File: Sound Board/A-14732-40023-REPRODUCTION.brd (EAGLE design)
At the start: 160 x 100 mm, 220 parts, among them P6 POWER, P7 SPEAKER, Q1 MPS3646, U1 OKI6295, U10 26LS32A, U11 26LS31, U12 27C040-150, U13 27C040-150, U14 YAMAHA 2151, U15 TIL7524, U16 74LS374, U17 74LS174, U18 16L8, U19 74LS11, U2 2064, U20 74LS139, U21 74LS14, U22 74LS74, U23 74LS74, U24 26LS31, U25 26LS32A, U26 74LS04, U28 YAMAHA 3012, U29 LM324D, U3 27C040, U30 MC3340, U31 MB3731, U32 TL084D, U33 TL084D, U4 6809E, U5 74LS374DW, U6 26LS32A, U7 26LS31, U8 74LS138, U9 74LS74, Y1 3.5749MHz, Y2 8MHz

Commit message: initial layout after autogeneration
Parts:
- VR1: device MK-ICs:7809-D2PAK -> MK-ICs:7809-TO220V
- moved P1 281.2 mm to (156.2, 76.2), turned to 270 degrees
- moved MTG1 271.6 mm to (158.8, 2.54)
- moved U31 268.3 mm to (157.5, 30.5), turned to 270 degrees
- moved MTG3 261.1 mm to (157.5, 96.5)
- moved L1 259.8 mm to (128.3, 17.8)
- moved L2 257.4 mm to (116.8, 17.8)
- moved RV1 239.1 mm to (105.4, 6.35), turned to 90 degrees
- moved U33 238.5 mm to (139.7, 47.0), turned to 270 degrees
- moved U18 237.8 mm to (119.4, 54.6), turned to 270 degrees
- moved U16 235.0 mm to (138.4, 61.0), turned to 270 degrees
- moved C95 230.5 mm to (137.2, 31.8), turned to 90 degrees
- moved U10 225.7 mm to (156.2, 52.1), turned to 270 degrees
- moved P7 223.8 mm to (149.9, 5.08)
- moved U5 218.7 mm to (137.2, 78.7), turned to 270 degrees
- moved U32 215.9 mm to (129.5, 47.0), turned to 270 degrees
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
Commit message: layout WIP
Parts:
- removed C79: 220uF, A-14732-40023:PANASONIC_E
- added C84: 220uF, A-14732-40023:PANASONIC_E
- RV1: device SparkFun-Electromechanical:ALPS_POT_KIT -> SparkFun-Electromechanical:POT_ALPHA_RV16AF-20
- U1: device MK-ICs:OKI6295 -> A-14732-40023:QFP44
- U12, U13, U3: device MK-ICs:27C040 -> A-14732-40023:PLCC-S32
- U14: device MK-ICs:YM2151 -> A-14732-40023:DIP24
- U18: device MK-ICs:16L8 -> A-14732-40023:DIP20N
- U2: device MK-ICs:MS6264L -> A-14732-40023:SOP28
- U28: device MK-ICs:YM3012 -> A-14732-40023:DIP16N
- Y1: device crystal:SM49 -> crystal:HC49U-V
- moved R92 133.6 mm to (148.8, 43.9), turned to 90 degrees
- moved R18 133.0 mm to (147.3, 63.2)
- moved C43 131.7 mm to (147.3, 66.0), turned to 180 degrees
- moved C48 130.4 mm to (4.57, 9.65)
- moved R17 129.6 mm to (147.8, 68.6)
- moved C42 129.1 mm to (147.8, 71.1), turned to 180 degrees
- moved R16 126.0 mm to (148.1, 73.2)
- moved C41 125.5 mm to (147.3, 74.7), turned to 180 degrees
- moved C47 124.9 mm to (12.7, 95.2)
- moved C12 124.1 mm to (7.87, 85.6)
- moved R15 122.6 mm to (147.6, 79.5), turned to 180 degrees
- moved C40 122.5 mm to (147.6, 77.0), turned to 180 degrees
- moved C7 121.9 mm to (128.8, 98.8), turned to 180 degrees
- moved C50 121.2 mm to (4.83, 15.0)
- moved C83 120.3 mm to (153.4, 43.4)
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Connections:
- net AGND: now also C84.-, RV1.1, RV1.2; no longer C79.-, RV1.P$2, RV1.P$3
- net N$87: now also RV1.3; no longer RV1.P$1
- net N$92: now also C84.+; no longer C79.+
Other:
- board size 160 x 100 mm -> 160 x 102.3 mm

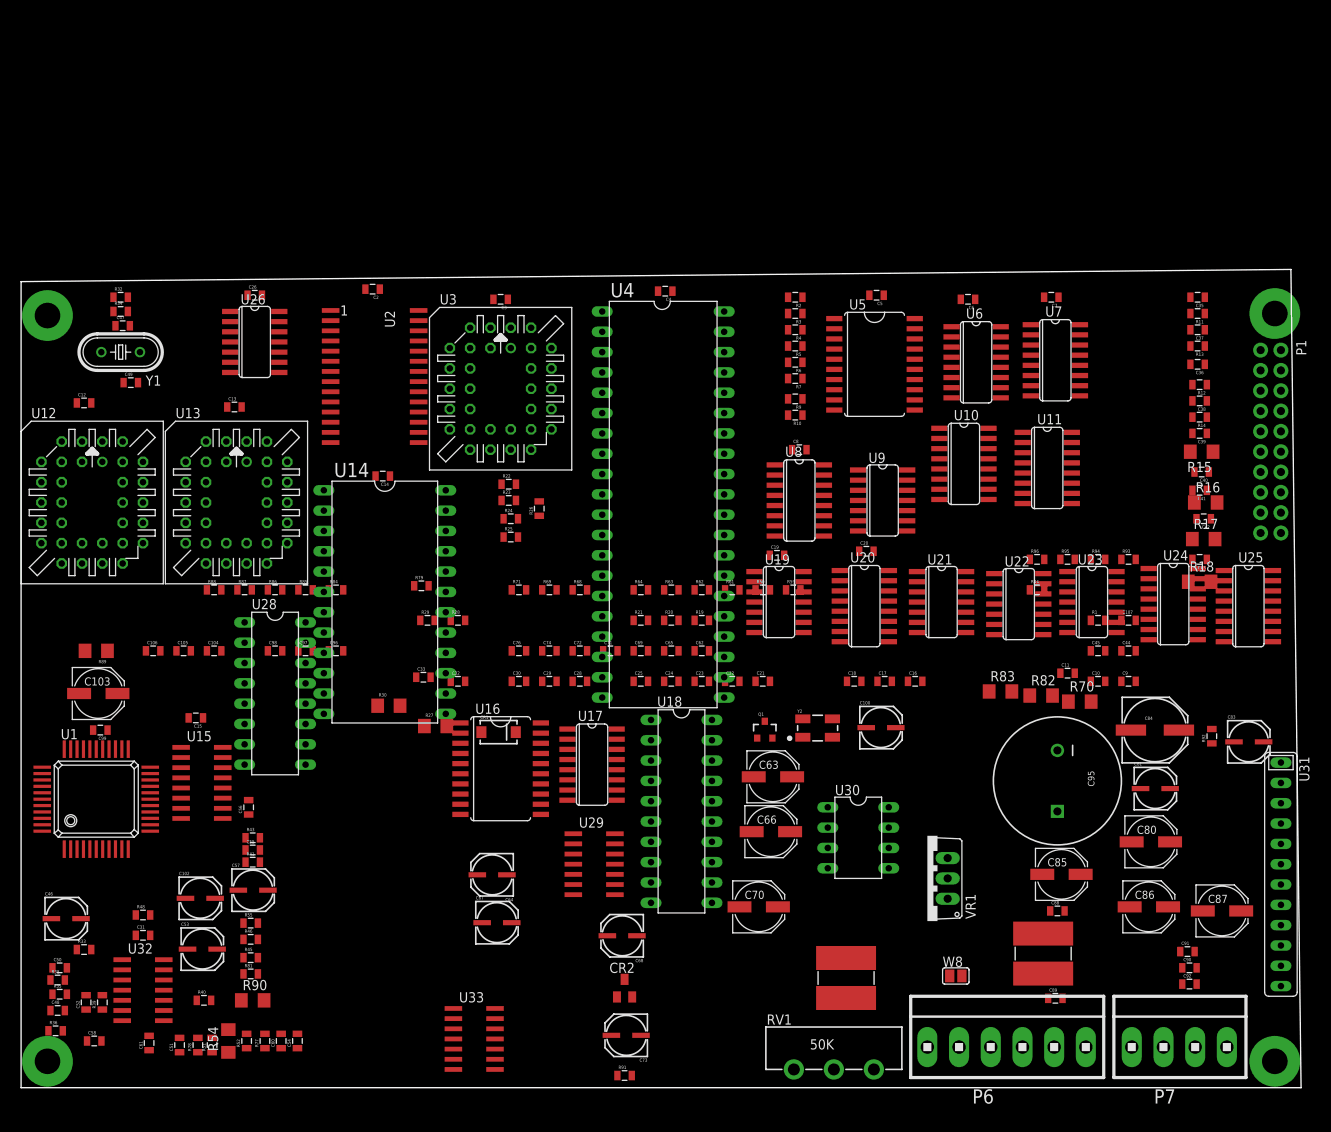
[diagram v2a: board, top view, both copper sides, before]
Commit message: Trying to lay around, resulting in fixing misplaced components and other fixes
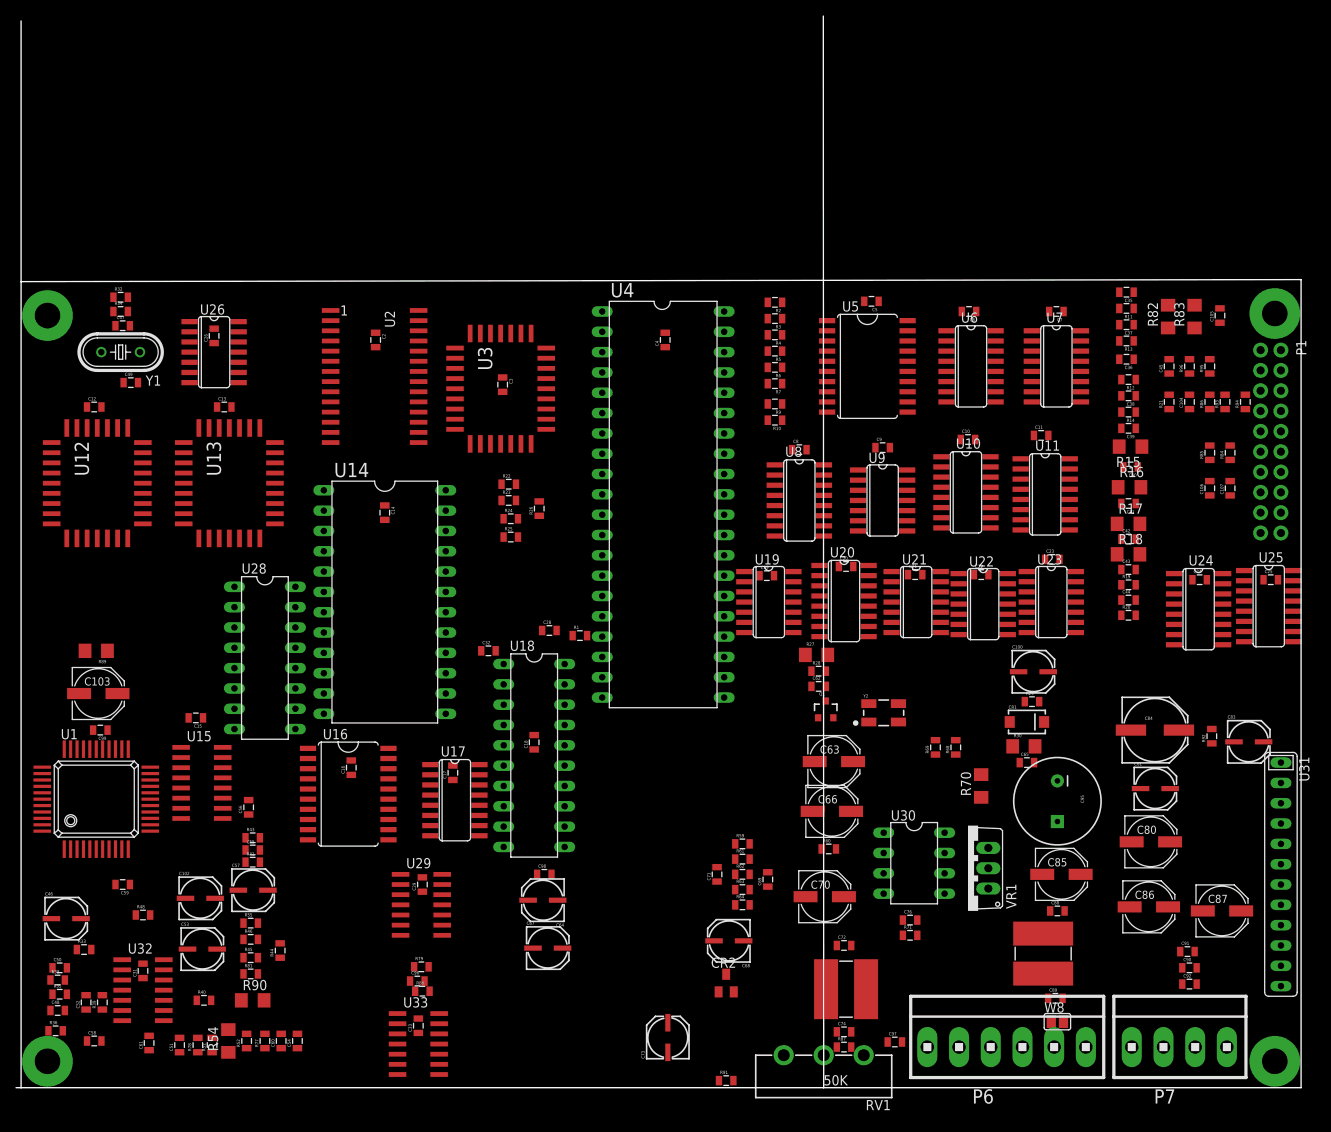
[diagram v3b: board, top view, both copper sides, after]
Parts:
- removed C30: 33pF, SparkFun-Passives:0805
- added C59: 33pF, SparkFun-Passives:0805
- C95: device A-14732-40023:CPOL-RADIAL-1000UF-63V -> A-14732-40023:CPOL-RADIAL-1000UF-25V
- U12, U13, U3: device A-14732-40023:PLCC-S32 -> A-14732-40023:PLCC32R
- moved C105 136.2 mm to (149.9, 96.5), turned to 90 degrees
- moved C106 133.6 mm to (148.6, 74.9), turned to 90 degrees
- moved C104 125.8 mm to (146.1, 85.7), turned to 90 degrees
- moved R86 119.2 mm to (148.6, 85.7), turned to 90 degrees
- moved R85 114.3 mm to (148.6, 79.4), turned to 90 degrees
- moved R84 113.1 mm to (151.1, 79.4), turned to 90 degrees
- moved R44 104.8 mm to (32.4, 17.1), turned to 90 degrees
- moved R87 94.2 mm to (102.9, 5.08)
- moved C97 88.4 mm to (109.2, 5.71)
- moved C25 79.8 mm to (156.2, 63.5)
- moved R30 79.5 mm to (125.3, 42.7)
- moved R29 76.2 mm to (126.4, 48.3)
- moved R21 71.5 mm to (143.5, 85.7), turned to 90 degrees
- moved C16 71.3 mm to (41.3, 40.0), turned to 90 degrees
- moved C24 67.3 mm to (147.3, 63.5)
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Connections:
- net N$79: now also C59.1; no longer C30.1
- net N$80: now also C59.2; no longer C30.2
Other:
- board size 160 x 102.3 mm -> 160.6 x 134 mm

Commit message: board layout wip
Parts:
- R15, R16, R17, R18: device resistor:R1206 -> SparkFun-Passives:0805
- Y1: device crystal:HC49U-V -> crystal:HC49UP
- moved C32 78.0 mm to (135.9, 45.7), turned to 270 degrees
- moved R1 53.5 mm to (34.3, 96.5), turned to 270 degrees
- moved C28 38.1 mm to (27.9, 57.1), turned to 90 degrees
- moved R86 27.9 mm to (158.8, 59.7)
- moved C59 26.4 mm to (27.9, 3.81), turned to 90 degrees
- moved C19 24.8 mm to (90.2, 39.4), flipped to the bottom, turned to 90 degrees
- moved R81 23.5 mm to (50.8, 6.35)
- moved R44 23.3 mm to (54.6, 10.2)
- moved R45 23.3 mm to (50.8, 8.89)
- moved R46 23.2 mm to (50.8, 11.4)
- moved R55 23.1 mm to (50.8, 14.0)
- moved C106 23.0 mm to (151.1, 97.8)
- moved C107 23.0 mm to (153.7, 97.8)
- moved R90 23.0 mm to (50.8, 3.81)
- moved C57 22.6 mm to (50.8, 19.1)
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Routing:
- net GND: track 0.00 -> 516.2 mm
- net SND_DAT3: track 0.00 -> 13.0 mm
- net SND_DAT1: track 0.00 -> 13.0 mm
- net SND_DAT4: track 0.00 -> 7.77 mm
- net B_SND_RD: track 0.00 -> 7.77 mm
- net SND_DAT6: track 0.00 -> 7.77 mm
- net SND_DAT2: track 0.00 -> 7.77 mm
- net SND_DAT0: track 0.00 -> 7.77 mm
- net N$101: track 0.00 -> 7.77 mm
- net SND_RDY: track 0.00 -> 6.72 mm
- net SND_DAV: track 0.00 -> 6.72 mm
- net N$99: track 0.00 -> 6.50 mm
- net N$102: track 0.00 -> 6.50 mm
- net SND_DAT7: track 0.00 -> 6.50 mm
- net SND_DAT5: track 0.00 -> 6.50 mm
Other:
- board size 160.6 x 134 mm -> 162.6 x 102.9 mm
